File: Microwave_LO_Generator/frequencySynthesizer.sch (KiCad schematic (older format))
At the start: 29 parts, among them J1 BNC_THT, J2 SMA_END, J3 SMA_END, U1 ADF4150HV, X1 IQXT-220-1

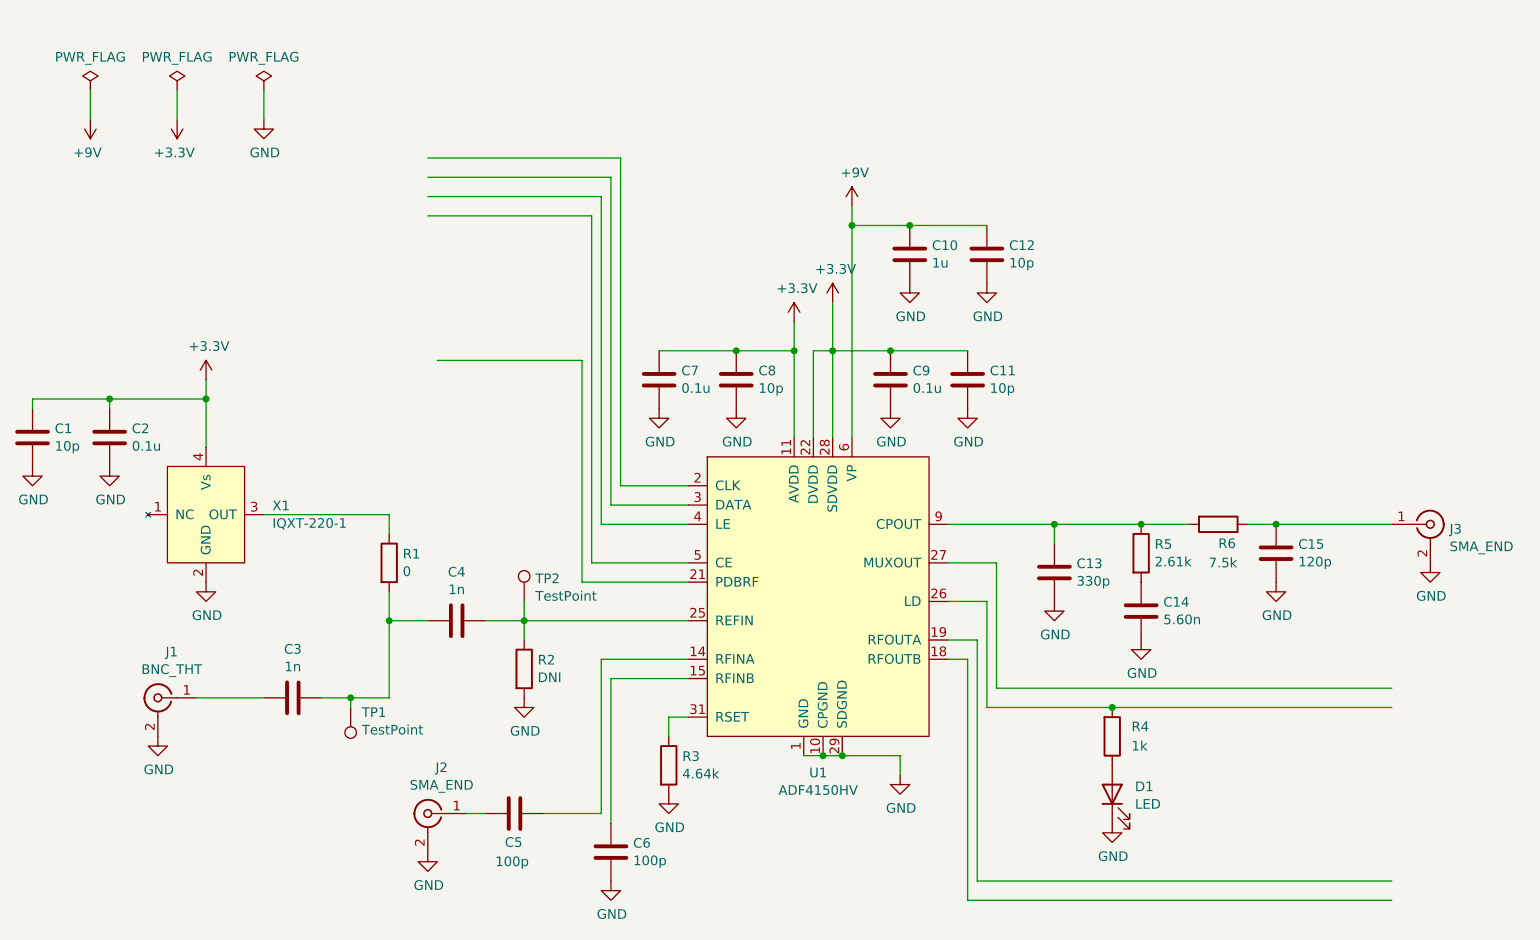
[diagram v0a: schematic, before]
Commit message: add vco
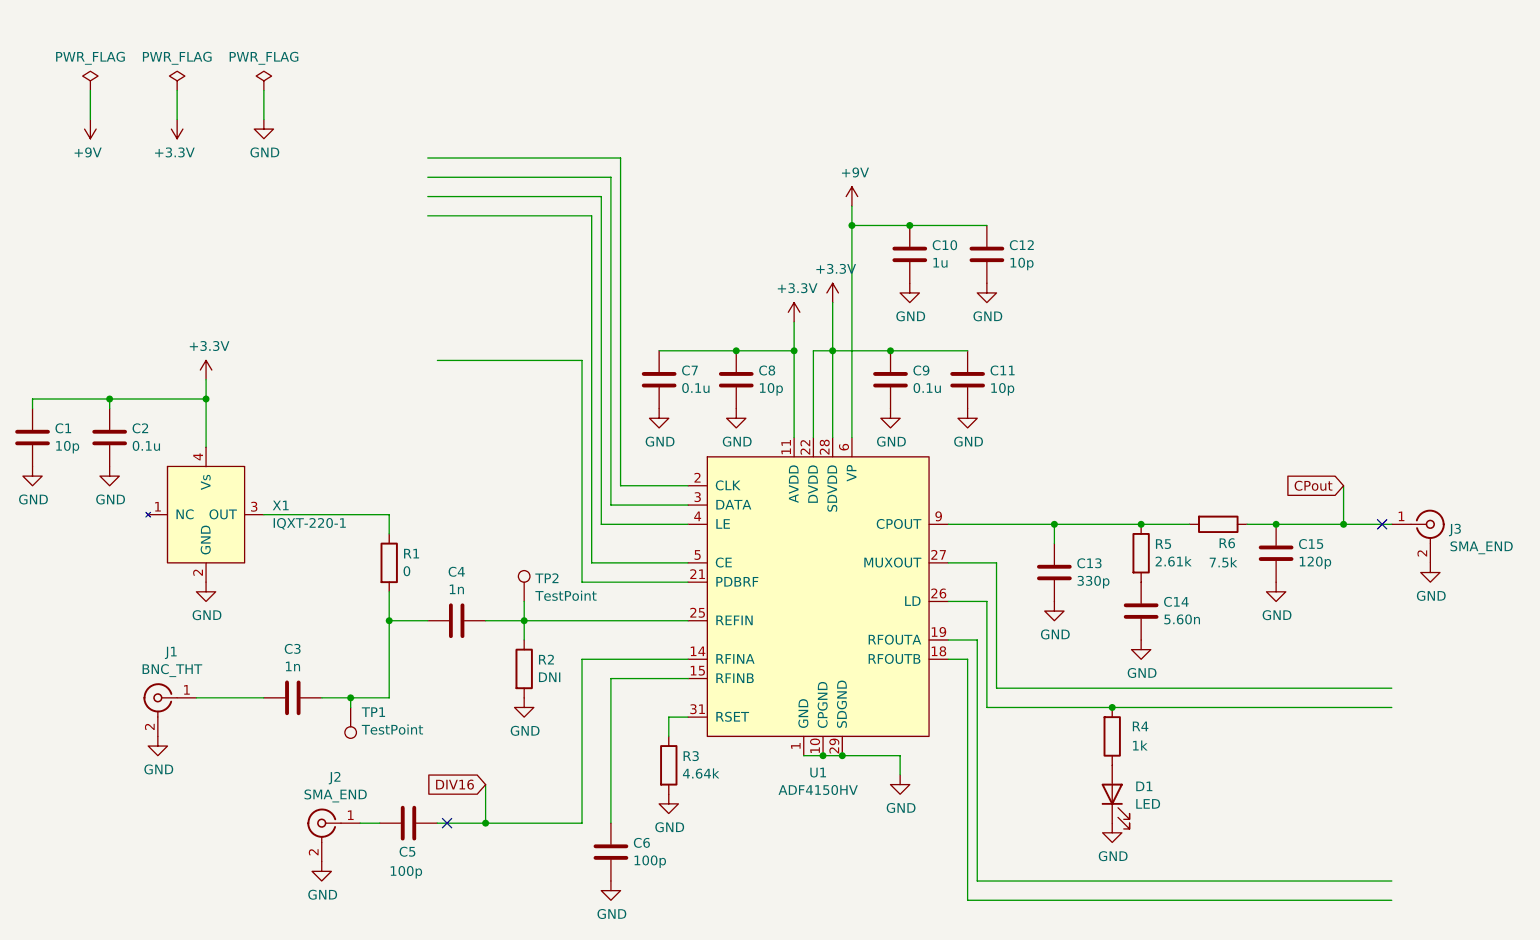
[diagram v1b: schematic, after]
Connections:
- net labels added: CPout, DIV16
- wire segments 82 -> 86
- no-connect marks 0 -> 2
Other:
- moved on the sheet: C5, J2

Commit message: Update and fix
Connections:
- net labels added: 0
- wire segments 86 -> 88
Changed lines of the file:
@@
 	1    0    0    -1
 $EndComp
+$Comp
+L power:GND #PWR0137
+U 1 1 5FC3AE3B
+P 2950 1050
+F 0 "#PWR0137" H 2950 800 50  0001 C CNN
+F 1 "GND" H 2955 877 50  0000 C CNN
+F 2 "" H 2950 1050 50  0001 C CNN
+F 3 "" H 2950 1050 50  0001 C CNN
+	1    2950 1050
+	1    0    0    -1
+$EndComp
+$Comp
+L pspice:0 #GND0121
+U 1 1 5FC3D38F
+P 3200 1100
+F 0 "#GND0121" H 3200 1000 50  0001 C CNN
+F 1 "0" H 3200 1189 50  0000 C CNN
+F 2 "" H 3200 1100 50  0001 C CNN
+F 3 "~" H 3200 1100 50  0001 C CNN
+	1    3200 1100
+	1    0    0    -1
+$EndComp
+Wire Wire Line
+	2950 1050 3200 1050
+Wire Wire Line
+	3200 1050 3200 1100
 $EndSCHEMATC

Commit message: Update
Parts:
- added J4: Conn_01x05_Male, Connector_PinHeader_2.54mm:PinHeader_1x05_P2.54mm_Vertical, symbol Connector:Conn_01x05_Male
- added R16: 0, Resistor_SMD:R_0402_1005Metric_Pad0.72x0.64mm_HandSolder, symbol Device:R
- added R17: DNI, Resistor_SMD:R_0603_1608Metric_Pad0.98x0.95mm_HandSolder, symbol Device:R
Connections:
- wire segments 88 -> 95
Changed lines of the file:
@@
 	2500 1350 2500 1500
-$Comp
-L power:+3.3V #PWR0103
-U 1 1 5FB52FA7
-P 5250 2550
-F 0 "#PWR0103" H 5250 2400 50  0001 C CNN
-F 1 "+3.3V" H 5265 2723 50  0000 C CNN
-F 2 "" H 5250 2550 50  0001 C CNN
-F 3 "" H 5250 2550 50  0001 C CNN
-	1    5250 2550
-	1    0    0    -1
-$EndComp
 $Comp
 L power:+9V #PWR0104
@@
 	5450 2450 5450 2700
 Wire Wire Line
-	5250 2550 5250 2700
-Wire Wire Line
 	5350 2700 5450 2700
 Connection ~ 5450 2700
@@
 	1    0    0    -1
 $EndComp
-Connection ~ 5250 2700
 Wire Wire Line
 	5250 2700 5250 3150
@@
 Wire Wire Line
 	3200 1050 3200 1100
+$Comp
+L pspice:0 #GND0122
+U 1 1 5FCD8892
+P 3750 1600
+F 0 "#GND0122" H 3750 1500 50  0001 C CNN
+F 1 "0" H 3750 1689 50  0000 C CNN
+F 2 "" H 3750 1600 50  0001 C CNN
+F 3 "~" H 3750 1600 50  0001 C CNN
+	1    3750 1600
+	1    0    0    -1
+$EndComp
+Wire Wire Line
+	3750 1500 3750 1600
+$Comp
+L Connector:Conn_01x05_Male J4
+U 1 1 5FCD328E
+P 3150 1800
+F 0 "J4" H 3258 2181 50  0000 C CNN
+F 1 "Conn_01x05_Male" H 3258 2090 50  0000 C CNN
+F 2 "Connector_PinHeader_2.54mm:PinHeader_1x05_P2.54mm_Vertical" H 3150 1800 50  0001 C CNN
+F 3 "~" H 3150 1800 50  0001 C CNN
+	1    3150 1800
+	1    0    0    -1
+$EndComp
+Wire Wire Line
+	3500 1500 3500 1600
+Wire Wire Line
+	3500 1600 3350 1600
+Wire Wire Line
+	3500 1500 3750 1500
+$Comp
+L Device:R R17
+U 1 1 5FD3B0E5
+P 3400 3000
+F 0 "R17" H 3470 3046 50  0000 L CNN
+F 1 "DNI" H 3470 2955 50  0000 L CNN
+F 2 "Resistor_SMD:R_0603_1608Metric_Pad0.98x0.95mm_HandSolder" V 3330 3000 50  0001 C CNN
+F 3 "~" H 3400 3000 50  0001 C CNN
+F 4 "D/CRCW0402 kit in dipartimento" H 3400 3000 50  0001 C CNN "Supplier Stock Code"
+	1    3400 3000
+	1    0    0    -1
+$EndComp
+Wire Wire Line
+	3400 3150 3400 3300
+Wire Wire Line
+	3400 2750 3400 2850
+$Comp
+L Device:R R16
+U 1 1 5FD46A04
+P 3400 2600
+F 0 "R16" H 3470 2646 50  0000 L CNN
+F 1 "0" H 3470 2555 50  0000 L CNN
+F 2 "Resistor_SMD:R_0402_1005Metric_Pad0.72x0.64mm_HandSolder" V 3330 2600 50  0001 C CNN
+F 3 "~" H 3400 2600 50  0001 C CNN
+F 4 "D/CRCW0402 kit in dipartimento" H 3400 2600 50  0001 C CNN "Supplier Stock Code"
+	1    3400 2600
+	1    0    0    -1
+$EndComp
+$Comp
+L pspice:0 #GND0123
+U 1 1 5FD49CF4
+P 3400 3300
+F 0 "#GND0123" H 3400 3200 50  0001 C CNN
+F 1 "0" H 3400 3389 50  0000 C CNN
+F 2 "" H 3400 3300 50  0001 C CNN
+F 3 "~" H 3400 3300 50  0001 C CNN
+	1    3400 3300
+	1    0    0    -1
+$EndComp
+Connection ~ 5250 2700
+Wire Wire Line
+	5250 2550 5250 2700
+$Comp
+L power:+3.3V #PWR0103
+U 1 1 5FB52FA7
+P 5250 2550
+F 0 "#PWR0103" H 5250 2400 50  0001 C CNN
+F 1 "+3.3V" H 5265 2723 50  0000 C CNN
+F 2 "" H 5250 2550 50  0001 C CNN
+F 3 "" H 5250 2550 50  0001 C CNN
+	1    5250 2550
+	1    0    0    -1
+$EndComp
+$Comp
+L power:+3.3V #PWR0138
+U 1 1 5FD4CD79
+P 3400 2300
+F 0 "#PWR0138" H 3400 2150 50  0001 C CNN
+F 1 "+3.3V" H 3415 2473 50  0000 C CNN
+F 2 "" H 3400 2300 50  0001 C CNN
+F 3 "" H 3400 2300 50  0001 C CNN
+	1    3400 2300
+	1    0    0    -1
+$EndComp
+Wire Wire Line
+	3400 2300 3400 2450
 $EndSCHEMATC

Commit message: Power Supply update
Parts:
- removed C3: 1n, Capacitor_SMD:C_0402_1005Metric_Pad0.74x0.62mm_HandSolder, symbol Device:C
- removed C5: 100p, Capacitor_SMD:C_0402_1005Metric_Pad0.74x0.62mm_HandSolder, symbol Device:C
- removed J1: BNC_THT, Connector_Coaxial:BNC_Amphenol_B6252HB-NPP3G-50_Horizontal, symbol frequencySynthesizer-rescue:BNC_THT-frequencySintesizer
- removed J2, J3: SMA_END, Connector_Coaxial:SMA_Molex_73251-1153_EdgeMount_Horizontal, symbol frequencySynthesizer-rescue:SMA_END-frequencySintesizer
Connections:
- wire segments 95 -> 92
- no-connect marks 2 -> 1
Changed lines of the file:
@@
 Wire Wire Line
 	3850 4100 4700 4100
-$Comp
-L Device:C C3
-U 1 1 5FBBE9A1
-P 2650 4500
-F 0 "C3" V 2398 4500 50  0000 C CNN
-F 1 "1n" V 2489 4500 50  0000 C CNN
-F 2 "Capacitor_SMD:C_0402_1005Metric_Pad0.74x0.62mm_HandSolder" H 2688 4350 50  0001 C CNN
-F 3 "~" H 2650 4500 50  0001 C CNN
-F 4 "GRM1555C1H102FA01D" H 2650 4500 50  0001 C CNN "Manufacturer/Part Number"
-F 5 "Mouser 81-GRM1555C1H102FA1D" H 2650 4500 50  0001 C CNN "Supplier Stock Code"
-	1    2650 4500
-	0    1    1    0
-$EndComp
-Wire Wire Line
-	2150 4500 2500 4500
-$Comp
-L power:GND #PWR0118
-U 1 1 5FB92468
-P 1950 4700
-F 0 "#PWR0118" H 1950 4450 50  0001 C CNN
-F 1 "GND" H 1955 4527 50  0000 C CNN
-F 2 "" H 1950 4700 50  0001 C CNN
-F 3 "" H 1950 4700 50  0001 C CNN
-	1    1950 4700
-	1    0    0    -1
-$EndComp
-$Comp
-L frequencySynthesizer-rescue:BNC_THT-frequencySintesizer J1
-U 1 1 5FB9ABFC
-P 1950 4500
-F 0 "J1" H 1878 4738 50  0000 C CNN
-F 1 "BNC_THT" H 1878 4647 50  0000 C CNN
-F 2 "Connector_Coaxial:BNC_Amphenol_B6252HB-NPP3G-50_Horizontal" H 1950 4500 50  0001 C CNN
-F 3 "https://www.te.com/commerce/DocumentDelivery/DDEController?Action=srchrtrv&DocNm=5227161&DocType=Customer+Drawing&DocLang=English&PartCntxt=5227161-1&DocFormat=pdf" H 1950 4500 50  0001 C CNN
-F 4 "5227161-1" H 1950 4500 50  0001 C CNN "Manufacturer/Part Number"
-F 5 "Mouser 571-5227161-1" H 1950 4500 50  0001 C CNN "Supplier Stock Code"
-	1    1950 4500
-	-1   0    0    -1
-$EndComp
 Wire Wire Line
 	4700 3400 4350 3400
@@
 	1    0    0    -1
 $EndComp
-$Comp
-L Device:C C5
-U 1 1 5FBE3534
-P 3250 5150
-F 0 "C5" V 3100 5200 50  0000 R CNN
-F 1 "100p" V 3000 5250 50  0000 R CNN
-F 2 "Capacitor_SMD:C_0402_1005Metric_Pad0.74x0.62mm_HandSolder" H 3288 5000 50  0001 C CNN
-F 3 "~" H 3250 5150 50  0001 C CNN
-F 4 "GCM1555C1H101JA16D" H 3250 5150 50  0001 C CNN "Manufacturer/Part Number"
-F 5 "Mouser 81-GCM1555C1H101JA6D" H 3250 5150 50  0001 C CNN "Supplier Stock Code"
-	1    3250 5150
-	0    -1   -1   0
-$EndComp
-Wire Wire Line
-	3000 5150 3100 5150
 Wire Wire Line
 	4300 4400 4300 5150
-$Comp
-L frequencySynthesizer-rescue:SMA_END-frequencySintesizer J2
-U 1 1 5FBFBE98
-P 2800 5150
-F 0 "J2" H 2728 5388 50  0000 C CNN
-F 1 "SMA_END" H 2728 5297 50  0000 C CNN
-F 2 "Connector_Coaxial:SMA_Molex_73251-1153_EdgeMount_Horizontal" H 2800 5150 50  0001 C CNN
-F 3 "https://www.mouser.it/datasheet/2/643/pi-CCS-JOHN-142-0701-851-1290383.pdf" H 2800 5150 50  0001 C CNN
-F 4 "142-0701-851" H 2800 5150 50  0001 C CNN "Manufacturer/Part Number"
-F 5 "Mouser 530-142-0701-851" H 2800 5150 50  0001 C CNN "Supplier Stock Code"
-	1    2800 5150
-	-1   0    0    -1
-$EndComp
-$Comp
-L power:GND #PWR0125
-U 1 1 5FBFF905
-P 2800 5350
-F 0 "#PWR0125" H 2800 5100 50  0001 C CNN
-F 1 "GND" H 2805 5177 50  0000 C CNN
-F 2 "" H 2800 5350 50  0001 C CNN
-F 3 "" H 2800 5350 50  0001 C CNN
-	1    2800 5350
-	1    0    0    -1
-$EndComp
 $Comp
 L power:GND #PWR0126
@@
 Wire Wire Line
 	5550 2050 5550 3150
-$Comp
-L power:GND #PWR0123
-U 1 1 5FBD07F2
-P 8550 3800
-F 0 "#PWR0123" H 8550 3550 50  0001 C CNN
-F 1 "GND" H 8555 3627 50  0000 C CNN
-F 2 "" H 8550 3800 50  0001 C CNN
-F 3 "" H 8550 3800 50  0001 C CNN
-	1    8550 3800
-	1    0    0    -1
-$EndComp
-$Comp
-L frequencySynthesizer-rescue:SMA_END-frequencySintesizer J3
-U 1 1 5FBCFA7F
-P 8550 3600
-F 0 "J3" H 8650 3575 50  0000 L CNN
-F 1 "SMA_END" H 8650 3484 50  0000 L CNN
-F 2 "Connector_Coaxial:SMA_Molex_73251-1153_EdgeMount_Horizontal" H 8550 3600 50  0001 C CNN
-F 3 "https://www.mouser.it/datasheet/2/643/pi-CCS-JOHN-142-0701-851-1290383.pdf" H 8550 3600 50  0001 C CNN
-F 4 "142-0701-851" H 8550 3600 50  0001 C CNN "Manufacturer/Part Number"
-F 5 "Mouser 530-142-0701-851" H 8550 3600 50  0001 C CNN "Supplier Stock Code"
-	1    8550 3600
-	1    0    0    -1
-$EndComp
 Wire Wire Line
 	8100 3600 8100 3400
-Connection ~ 8100 3600
-Wire Wire Line
-	8100 3600 8350 3600
 Text GLabel 8100 3400 0    50   Input ~ 0
 CPout
@@
 Wire Wire Line
 	3400 5150 3650 5150
-NoConn ~ 8300 3600
 NoConn ~ 3450 5150
 Text GLabel 3650 4950 0    50   Input ~ 0
